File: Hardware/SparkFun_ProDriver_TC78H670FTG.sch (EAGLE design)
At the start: 46 parts, among them J1 POWER_JACKTOE, J2 LATCH, J3 PTH, J4 LATCH, J5 LATCH, J6 PTH, J7 LATCH, J8 PTH, U1 TC78H670FTG, U2 LM1117

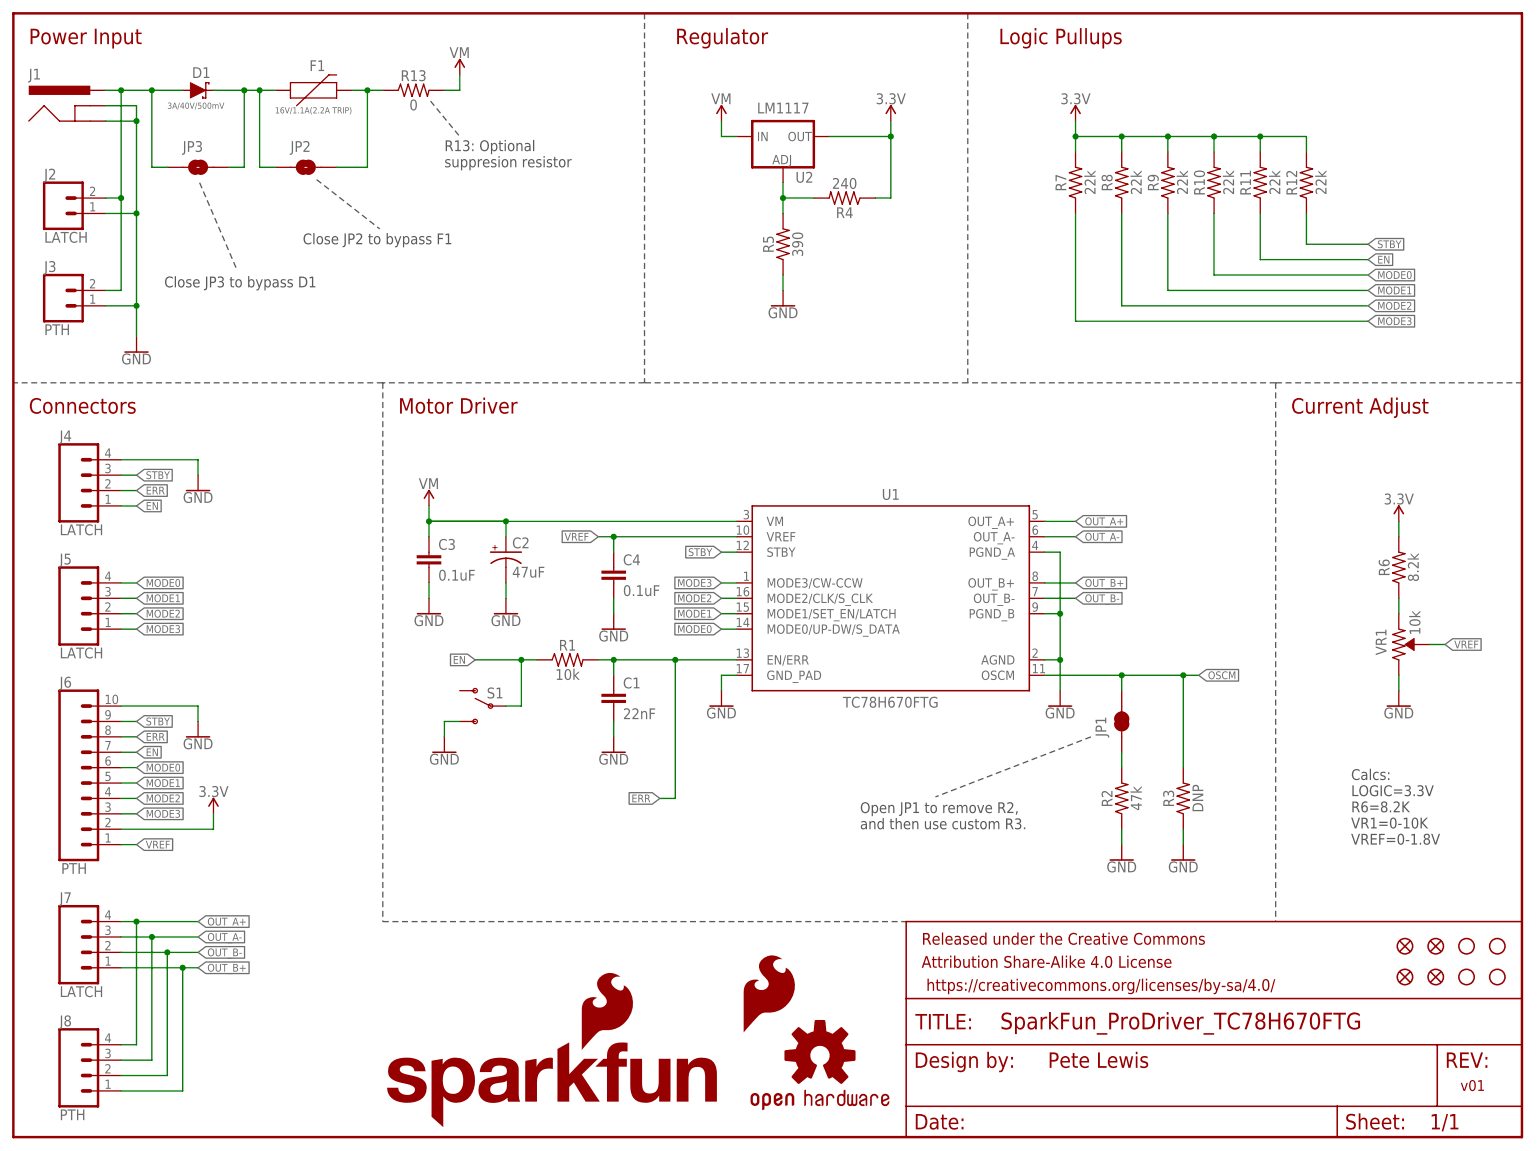
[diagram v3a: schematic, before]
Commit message: first run of checklist catches (pre-design review)
-4-layer board warnings in sch, brd, plus 1,2,3,4 in coppers
-added power LED
-added specail ordering instructions for 4-layer and 2 oz copper
-added measures
-ERR and STBY labels show active low overline now
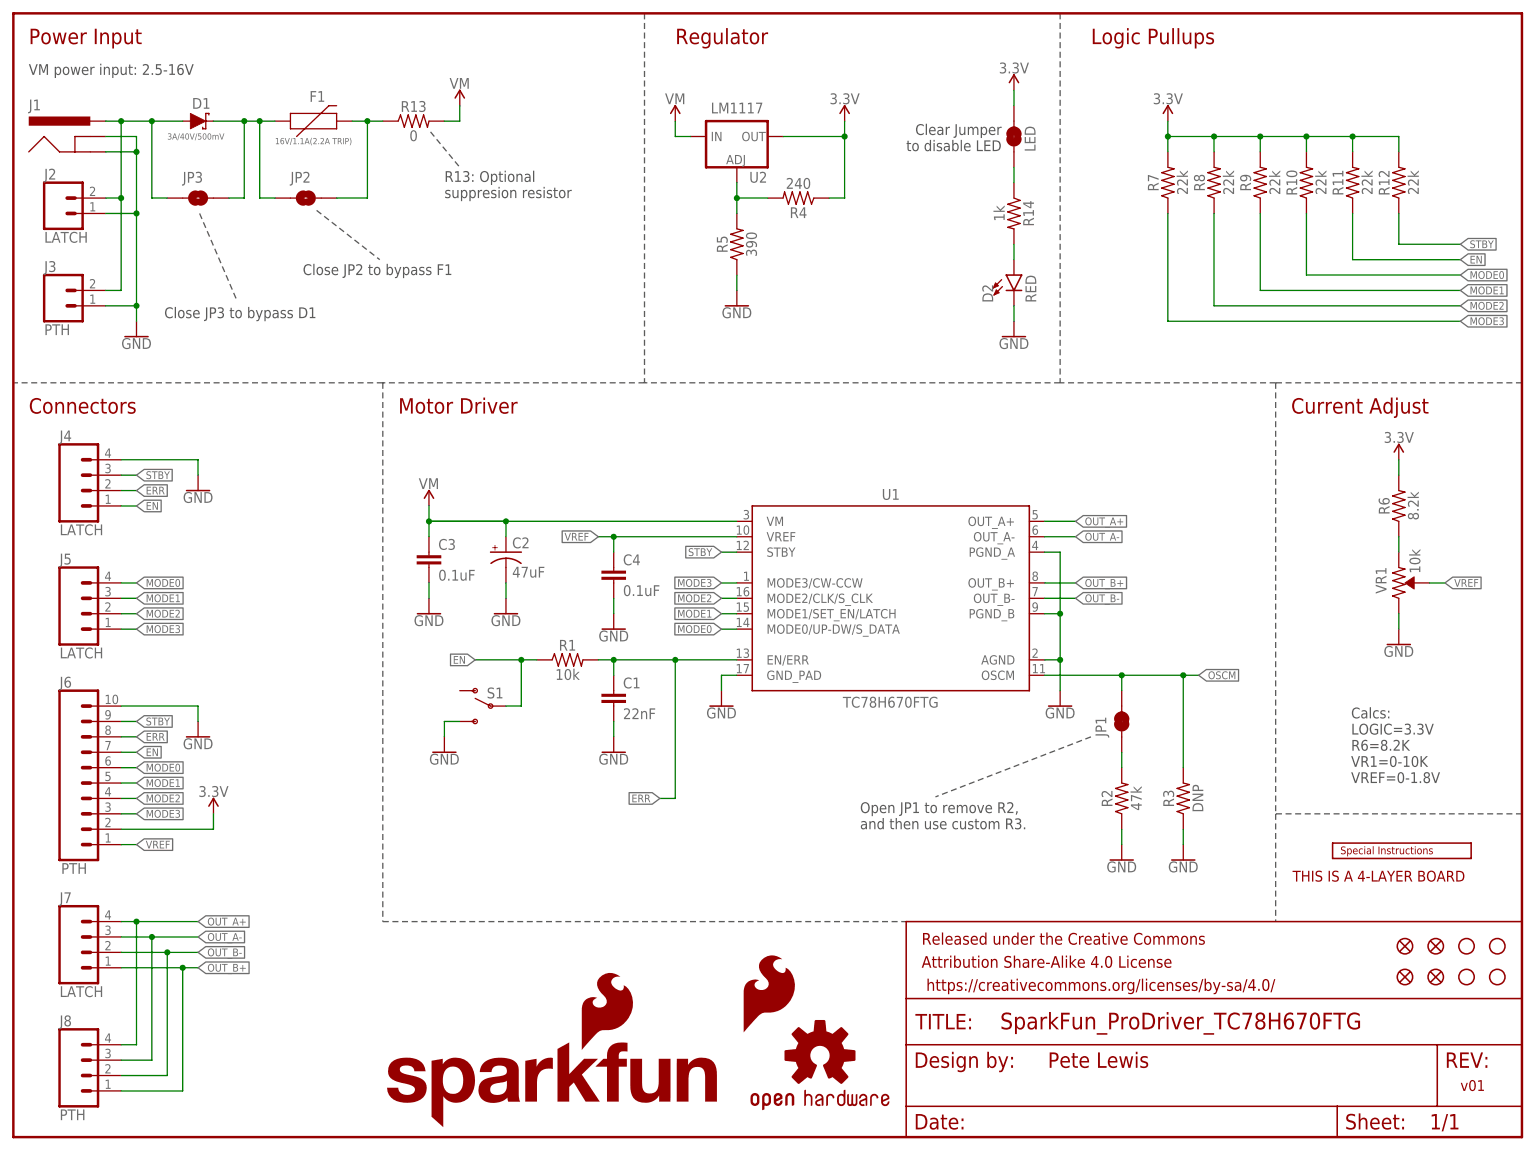
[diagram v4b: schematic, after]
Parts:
- added D2: RED, SparkFun-LED:LED-RED0603
- added JP4: LED, SparkFun-Jumpers:JUMPER-SMT_2_NC_TRACE_SILK
- added LOGO3: SPECIAL_INSTRUCTIONS-ORDERING, SparkFun-Aesthetics:SPECIAL_INSTRUCTIONS-ORDERING
- added R14: 1k, SparkFun-Resistors:1KOHM-0603-1/10W-1%
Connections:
- new net N$6: D2.A, R14.2
- new net N$8: JP4.1, R14.1
- net 3.3V: now also JP4.2
- net GND: now also D2.C
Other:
- note added: "Clear Jumper to disable LED"
- note added: "THIS IS A 4-LAYER BOARD"
- note added: "VM power input: 2.5-16V"
- moved on the sheet: D1, F1, J1, JP2, JP3, R10, R11, R12, R13, R4, R5, R6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

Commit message: ERR and STBY NET names to active low - now with overline
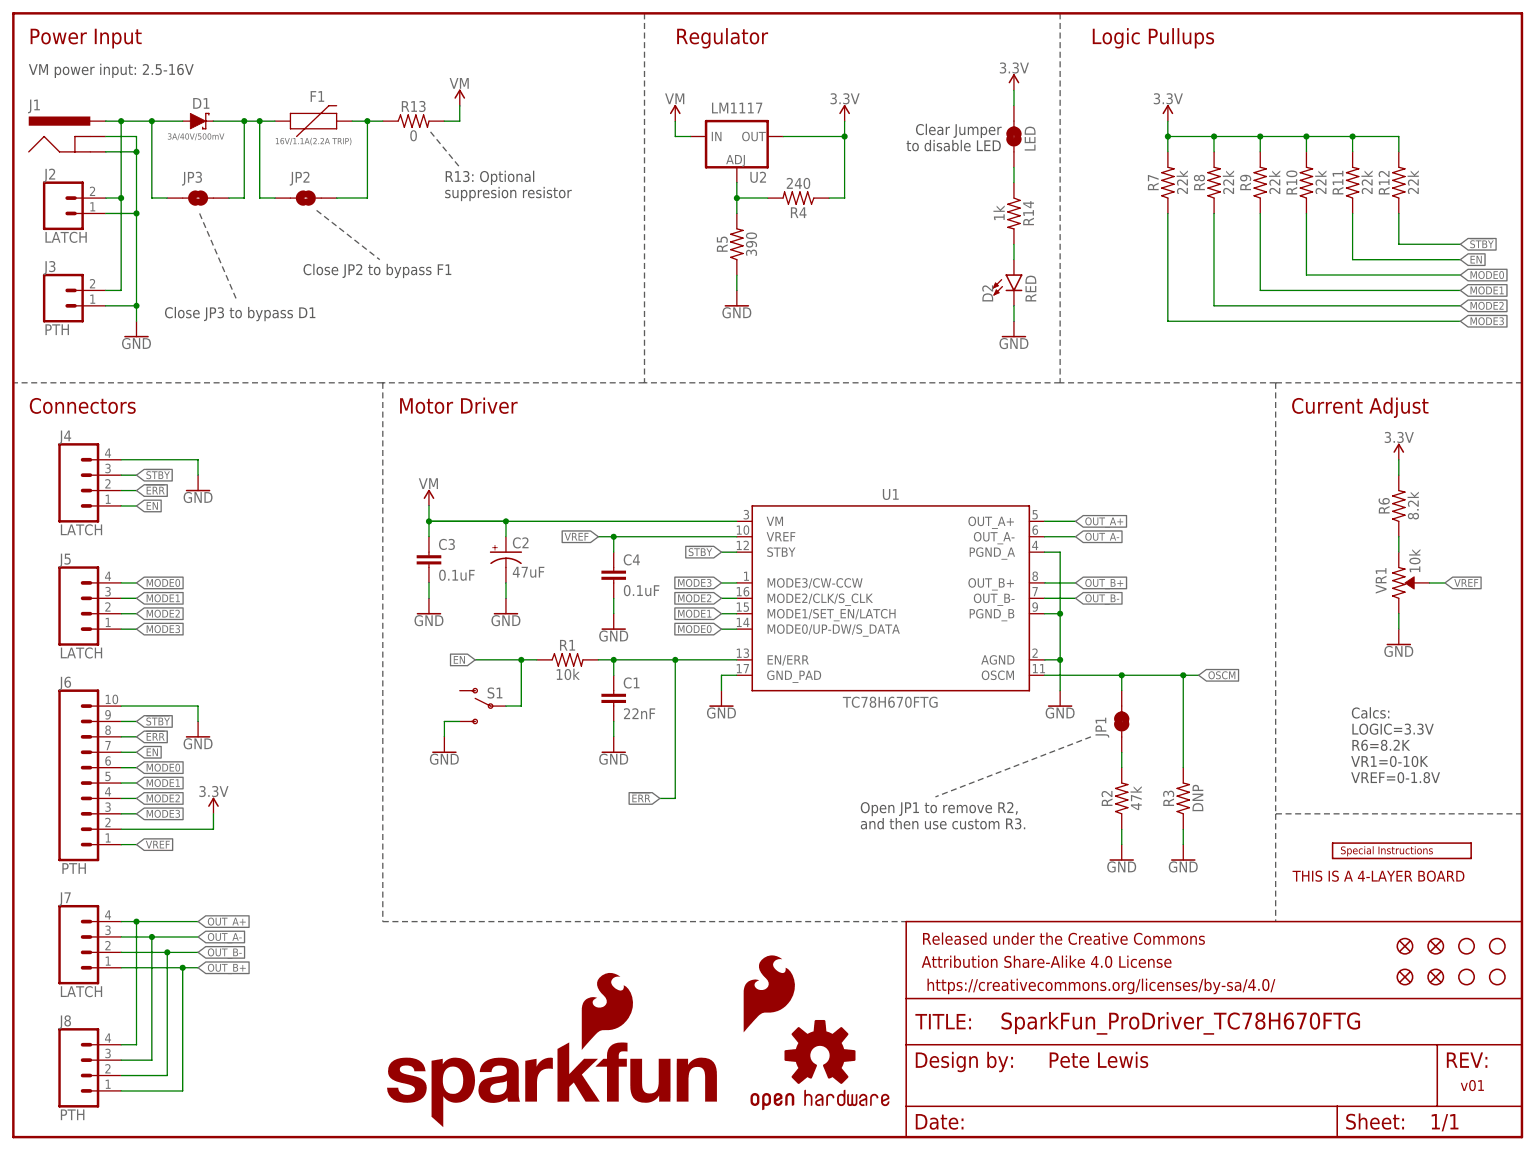
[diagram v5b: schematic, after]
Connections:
- net ERR renamed !ERR
- net STBY renamed !STBY
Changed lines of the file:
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@@
 </segment>
 </net>
-<net name="STBY" class="0">
+<net name="!STBY" class="0">
 <segment>
 <pinref part="U1" gate="G$1" pin="STBY"/>
@@
 </segment>
 </net>
-<net name="ERR" class="0">
+<net name="!ERR" class="0">
 <segment>
 <pinref part="U1" gate="G$1" pin="EN/ERR"/>

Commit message: Moved to pull-downs on EN and STBY
Because the powerup sequence requires that EN and STBY be low (while VM comes up), we should default these to low. Then the user can wire up these lines to their micro and write them HIGH when necessary.
-Adjusted how the enable hardware slide switch works. Now it simply disconnects the "user" control, so that it lets the pull-down resistor take effect. In this way, it will overide any logic level the user has provided on EN.
-Changes enable switch silk label to "user" indicating that the user must now provide logic control on the latch terminals or PTH headers.
-Added note in schematic about logic level tolerances
-re routed and moves some traces to maintain better top copper flow.
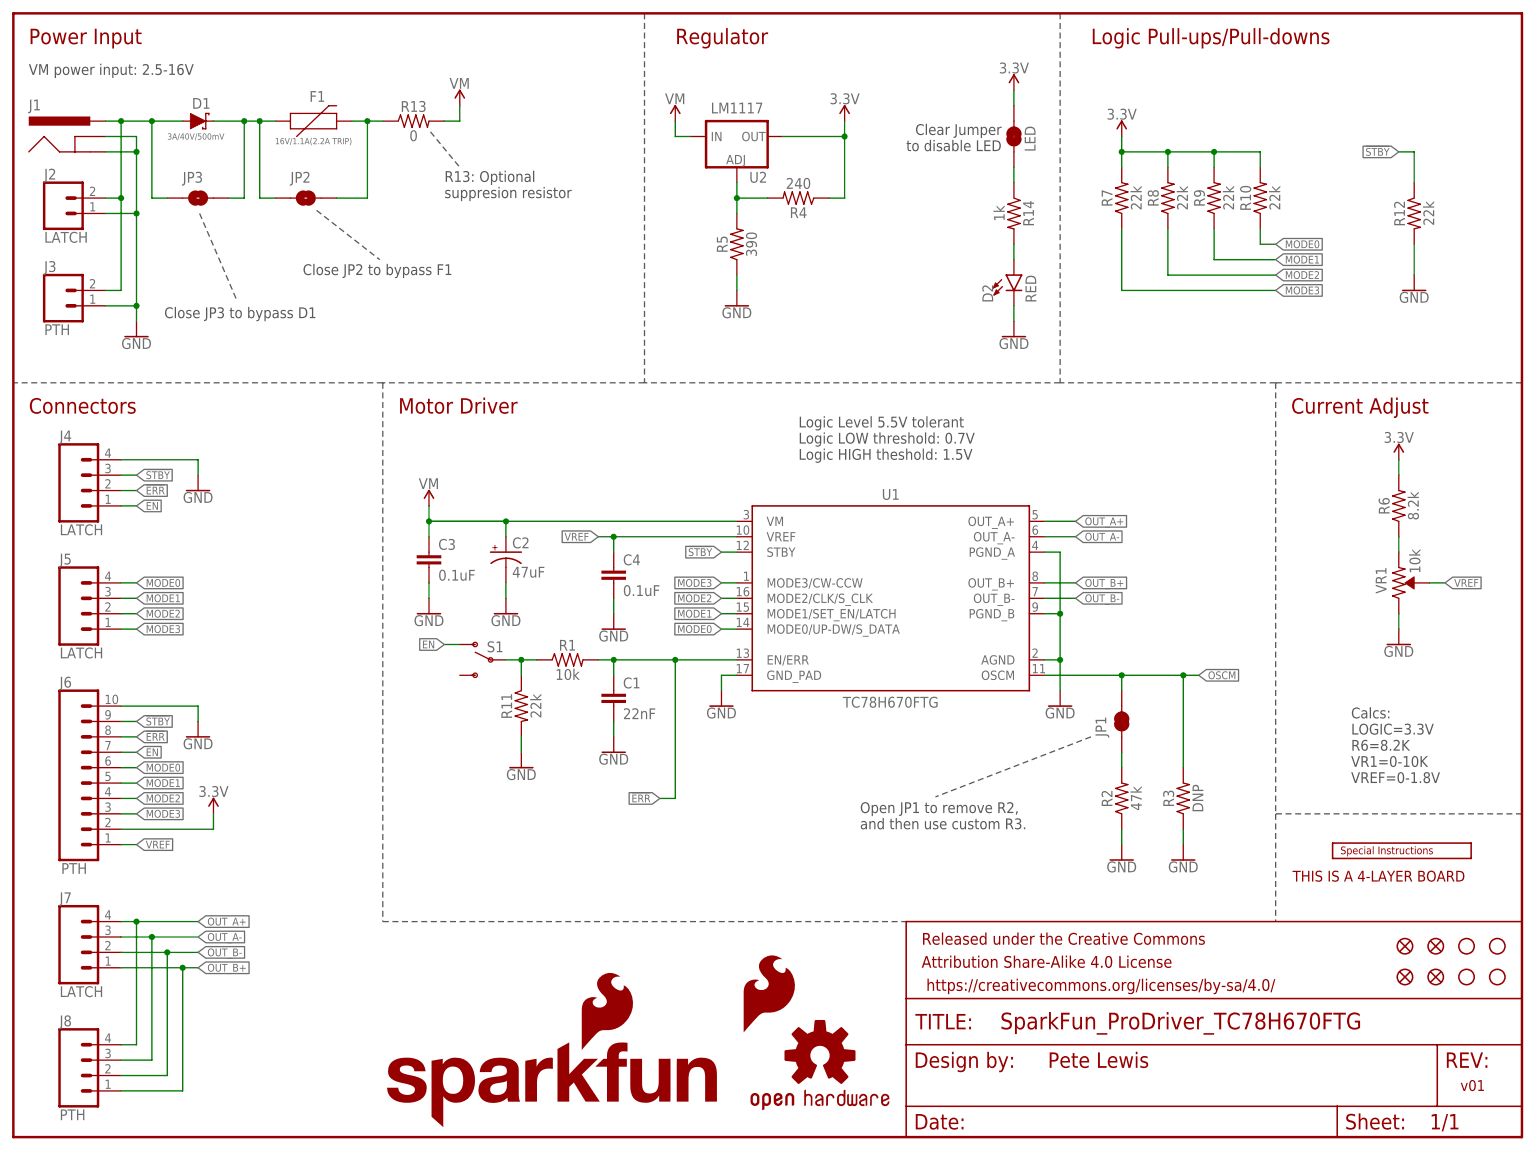
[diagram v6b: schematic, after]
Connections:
- new net N$7: R1.1, R11.1, S1.P
- net 3.3V: no longer R11.2, R12.2
- net EN: now also S1.O; no longer R1.1, R11.1, S1.P
- net GND: now also R11.2, R12.2; no longer S1.S
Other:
- note added: "Logic Level 5.5V tolerant Logic LOW threshold: 0.7V Logic HIGH theshold: 1.5V"
- note added: "Logic Pull-ups/Pull-downs"
- note removed: "Logic Pullups"
- moved on the sheet: R10, R11, R12, R7, R8, R9, S1
